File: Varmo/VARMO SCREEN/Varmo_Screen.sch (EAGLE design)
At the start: 34 parts, among them T1 MMBT2222AL, U1 LT1813CS8, U5 90814-0210

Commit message: Add PCA9670 to the schematic
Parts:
- removed R46, R47: 4.7k, rcl:R-EU_R0603
- added R20, R21: 4.7k, rcl:R-EU_R0603
- added R7: 100R, rcl:R-EU_R0603
- added U2: LT1813CS8, lineartechnology:LT1813CS8
- R1: value 100R -> 4.7k
- U1: value LT1813CS8 -> PCA9670D; device lineartechnology:LT1813CS8 -> NXP:PCA9670D
- renumbered C10 to C7, C4 to C1, C5 to C2, C6 to C3, C9 to C8, LCD1 to LCD2, LED6 to LED1, LED7 to LED2, LED8 to LED3, LED9 to LED4, R2 to R8, R25 to R13, R26 to R14, R29 to R15, R3 to R9, R30 to R16, R31 to R17, R4 to R10, R44 to R18, R45 to R19, R48 to R22, R49 to R23, R5 to R11, R50 to R24, R51 to R27, R6 to R12, T1 to T2, U$5 to U$1, U$7 to U$2, U5 to U3
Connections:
- removed net N$14: R10.2, R9.1, U1B.IN-
- removed net N$17: R10.1, R11.2, U1B.OUT
- removed net N$2: C1.1, R1.2, T2.B
- removed net N$3: R8.1, T2.C, U1A.IN+
- removed net N$5: R9.2, U1A.IN-, U1A.OUT
- new net N$1: C1.1, R7.2, T2.B
- new net N$6: R8.1, T2.C, U2A.IN+
- new net N$7: R9.2, U2A.IN-, U2A.OUT
- new net N$8: R10.2, R9.1, U2B.IN-
- new net N$9: R10.1, R11.2, U2B.OUT
- new net RESET: R1.1, U1.!RESET
- net +3V3: now also R1.2, R20.2, R21.2, U1.VDD; no longer R46.2, R47.2
- net +5V/1: now also U2A.V+; no longer U1A.V+
- net D0: now also U1.P0
- net D1: now also U1.P1
- net D2: now also U1.P2
- net D3: now also U1.P3
- net D4: now also U1.P4
- net D5: now also U1.P5
- net D6: now also U1.P6
- net D7: now also U1.P7
- net GND1: now also U1.AD0, U1.AD1, U1.VSS, U2B.IN+; no longer U1B.IN+
- net PWM_CONTRASTE: now also R7.1; no longer R1.1
- net SCL: now also R21.1, U1.SCL; no longer R47.1
- net SDA: now also R20.1, U1.SDA; no longer R46.1
- net VEE: now also U2A.V-; no longer U1A.V-
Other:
- note added: "I2C Adresse : 20h"

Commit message: Re routing the board
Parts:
- removed R20, R21: 4.7k, rcl:R-EU_R0603
- added R46, R47: 4.7k, rcl:R-EU_R0603
- R1: value 4.7k -> 100R
- R7: value 100R -> 4.7k
- U1: value PCA9670D -> LT1813CS8; device NXP:PCA9670D -> lineartechnology:LT1813CS8
- U2: value LT1813CS8 -> PCA9670D; device lineartechnology:LT1813CS8 -> NXP:PCA9670D
- renumbered C1 to C4, C2 to C5, C3 to C6, C7 to C10, C8 to C9, LCD2 to LCD1, LED1 to LED6, LED2 to LED7, LED3 to LED8, LED4 to LED9, R10 to R4, R11 to R5, R12 to R6, R13 to R25, R14 to R26, R15 to R29, R16 to R30, R17 to R31, R18 to R44, R19 to R45, R22 to R48, R23 to R49, R24 to R50, R27 to R51, R8 to R2, R9 to R3, T2 to T1, U$1 to U$5, U$2 to U$7, U3 to U5
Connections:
- removed net N$6: R2.1, T1.C, U2A.IN+
- removed net N$7: R3.2, U2A.IN-, U2A.OUT
- removed net N$8: R3.1, R4.2, U2B.IN-
- removed net N$9: R4.1, R5.2, U2B.OUT
- removed net RESET: R1.1, U1.!RESET
- new net N$14: R3.1, R4.2, U1B.IN-
- new net N$17: R4.1, R5.2, U1B.OUT
- new net N$2: C4.1, R1.2, T1.B
- new net N$3: R2.1, T1.C, U1A.IN+
- new net N$5: R3.2, U1A.IN-, U1A.OUT
- net +3V3: now also R46.2, R47.2, R7.2, U2.VDD; no longer R1.2, R20.2, R21.2, U1.VDD
- net +5V/1: now also U1A.V+; no longer U2A.V+
- net D0: now also U2.P0; no longer U1.P0
- net D1: now also U2.P1; no longer U1.P1
- net D2: now also U2.P2; no longer U1.P2
- net D3: now also U2.P3; no longer U1.P3
- net D4: now also U2.P4; no longer U1.P4
- net D5: now also U2.P5; no longer U1.P5
- net D6: now also U2.P6; no longer U1.P6
- net D7: now also U2.P7; no longer U1.P7
- net GND1: now also U1B.IN+, U2.AD0, U2.AD1, U2.AD2, U2.VSS; no longer U1.AD0, U1.AD1, U1.VSS, U2B.IN+
- net N$1: now also R7.1, U2.!RESET; no longer C4.1, R7.2, T1.B
- net PWM_CONTRASTE: now also R1.1; no longer R7.1
- net SCL: now also R47.1, U2.SCL; no longer R21.1, U1.SCL
- net SDA: now also R46.1, U2.SDA; no longer R20.1, U1.SDA
- net VEE: now also U1A.V-; no longer U2A.V-
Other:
- moved on the sheet: R1, R7

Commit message: Update the LT1813 devide
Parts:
- U1: value LT1813CS8 -> LT1813; device lineartechnology:LT1813CS8 -> lineartechnology:LT1813
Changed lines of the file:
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@@
 <parts>
 <part name="FRAME2" library="frames" deviceset="A3L-LOC" device=""/>
-<part name="U1" library="lineartechnology" deviceset="LT1813" device="CS8"/>
+<part name="U1" library="lineartechnology" deviceset="LT1813" device=""/>
 <part name="T1" library="transistor" deviceset="MMBT2222AL" device=""/>
 <part name="R1" library="rcl" deviceset="R-EU_" device="R0603" value="100R"/>

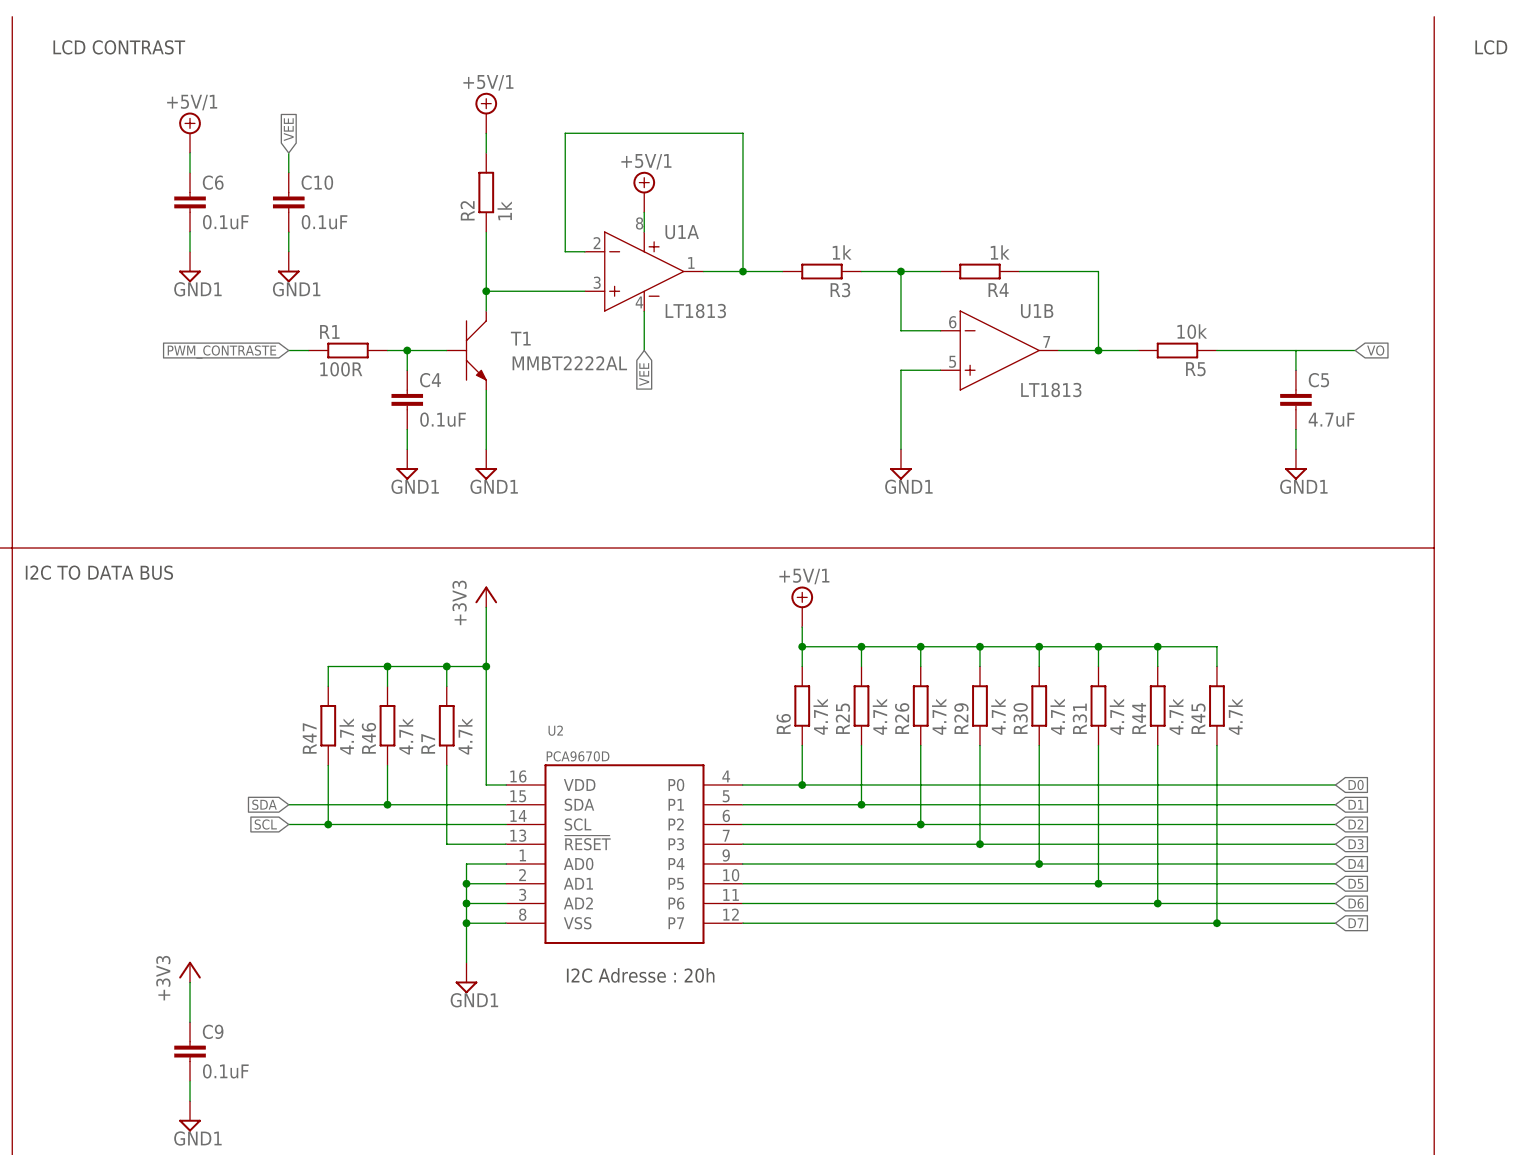
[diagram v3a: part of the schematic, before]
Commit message: Add TLP0401A to the schematic and route the board
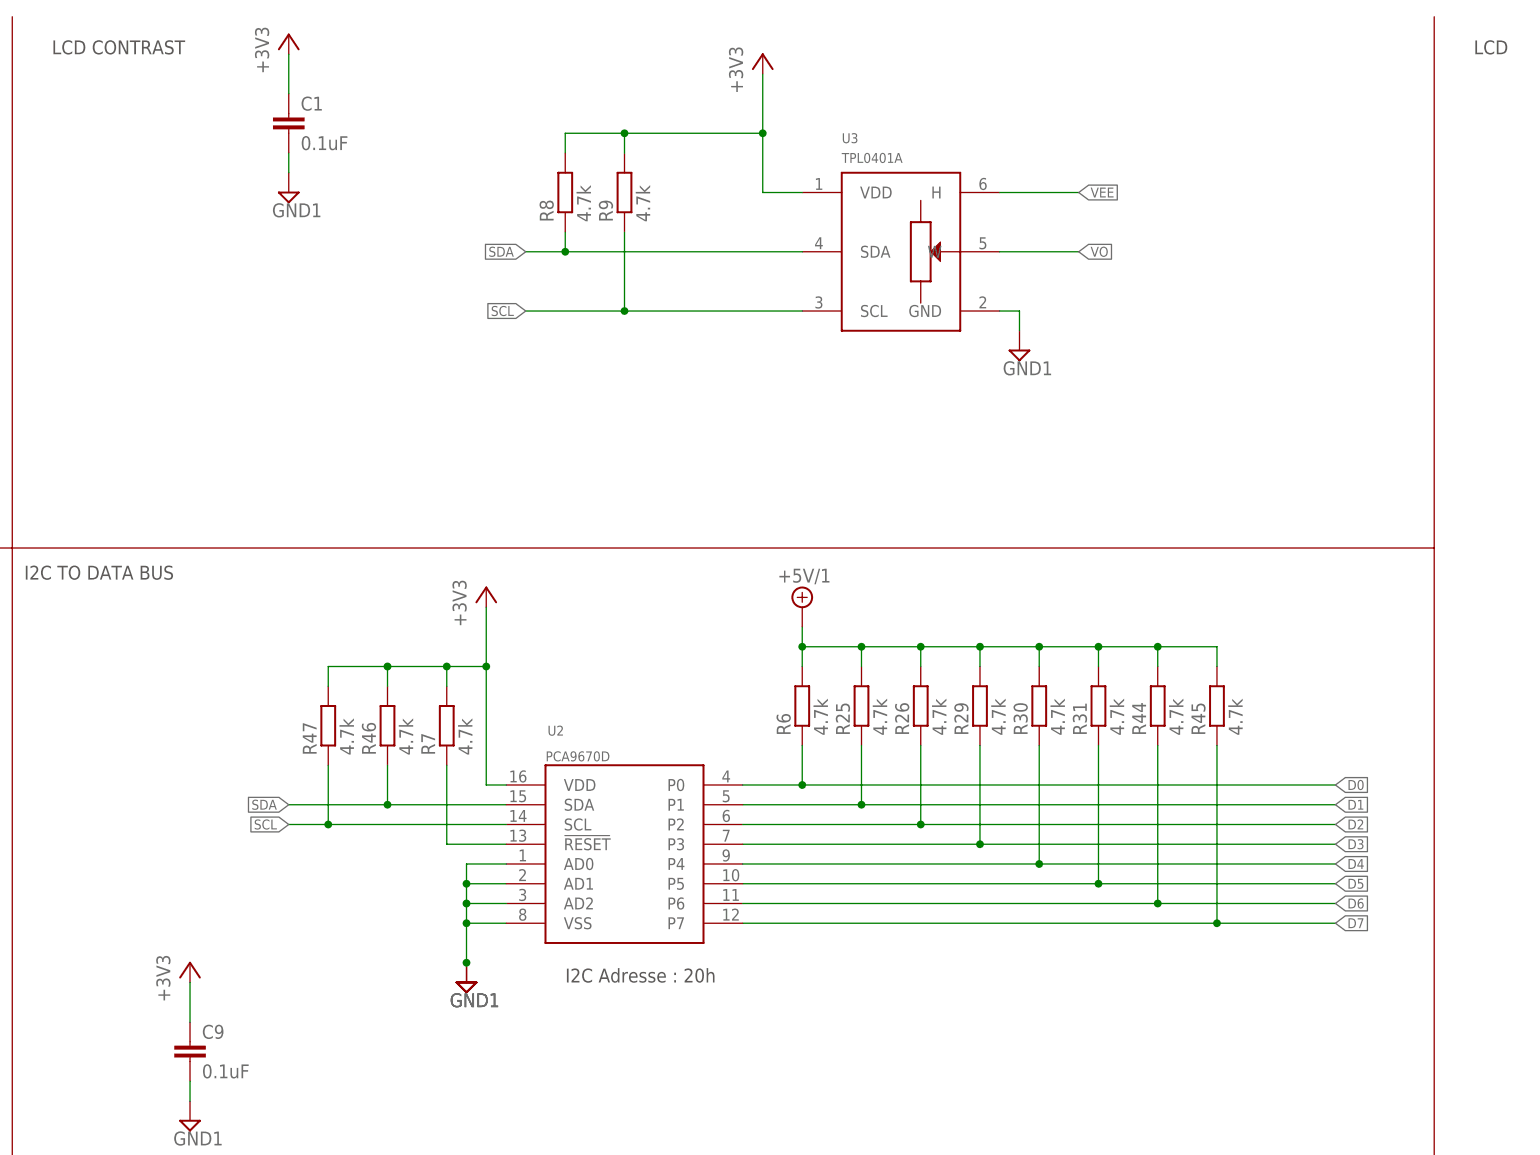
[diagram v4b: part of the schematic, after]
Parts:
- removed C10, C4, C6: 0.1uF, rcl:C-EUC0603
- removed C5: 4.7uF, rcl:C-EUC0603
- removed R1: 100R, rcl:R-EU_R0603
- removed R2, R3, R4: 1k, rcl:R-EU_R0603
- removed R5: 10k, rcl:R-EU_R0603
- removed T1: MMBT2222AL, transistor:MMBT2222AL
- removed U1: LT1813, lineartechnology:LT1813
- added C1: 0.1uF, rcl:C-EUC0603
- added R8, R9: 4.7k, rcl:R-EU_R0603
- added U3: TPL0401A, ti:TPL0401A
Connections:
- removed net N$14: R3.1, R4.2, U1B.IN-
- removed net N$17: R4.1, R5.2, U1B.OUT
- removed net N$2: C4.1, R1.2, T1.B
- removed net N$3: R2.1, T1.C, U1A.IN+
- removed net N$5: R3.2, U1A.IN-, U1A.OUT
- net +3V3: now also C1.1, R8.2, R9.2, U3.VDD
- net +5V/1: no longer C6.1, R2.2, U1A.V+
- net GND1: now also C1.2, U3.GND; no longer C10.2, C4.2, C5.2, C6.2, T1.E, U1B.IN+
- net PWM_CONTRASTE: no longer R1.1
- net SCL: now also R9.1, U3.SCL
- net SDA: now also R8.1, U3.SDA
- net VEE: now also U3.H; no longer C10.1, U1A.V-
- net VO: now also U3.W; no longer C5.1, R5.1

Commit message: Add manuel potentiometer
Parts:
- added R1: 3313J-1-103E, pot:3313J-1-103E
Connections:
- net GND1: now also R1.A
- net VEE: now also R1.E
- net VO: now also R1.S
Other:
- note added: "I2C Adresse : 2Eh"
- note added: "NC"
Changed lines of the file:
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@@
 <part name="R8" library="rcl" deviceset="R-EU_" device="R0603" value="4.7k"/>
 <part name="R9" library="rcl" deviceset="R-EU_" device="R0603" value="4.7k"/>
+<part name="R1" library="pot" deviceset="3313J" device="" technology="-1-103E"/>
+<part name="SUPPLY4" library="supply2" deviceset="GND1" device=""/>
 </parts>
 <sheets>
@@
 <text x="292.1" y="251.46" size="1.778" layer="97">LCD</text>
 <text x="175.26" y="132.08" size="1.778" layer="97">I2C Adresse : 20h</text>
+<text x="210.82" y="203.2" size="1.778" layer="97">I2C Adresse : 2Eh</text>
+<text x="266.7" y="223.52" size="1.778" layer="97">NC</text>
 </plain>
 <instances>
@@
 <instance part="R8" gate="G$1" x="175.26" y="233.68" rot="R90"/>
 <instance part="R9" gate="G$1" x="182.88" y="233.68" rot="R90"/>
+<instance part="R1" gate="G$1" x="264.16" y="228.6"/>
+<instance part="SUPPLY4" gate="G$1" x="264.16" y="213.36"/>
 </instances>
 <busses>
@@
 <label x="241.3" y="226.06" size="1.27" layer="95" xref="yes"/>
 <pinref part="U3" gate="G$1" pin="W"/>
+</segment>
+<segment>
+<wire x1="274.32" y1="228.6" x2="269.24" y2="228.6" width="0.1524" layer="91"/>
+<pinref part="R1" gate="G$1" pin="S"/>
+<label x="274.32" y="228.6" size="1.27" layer="95" xref="yes"/>
 </segment>
 </net>
@@
 <wire x1="139.7" y1="236.22" x2="139.7" y2="238.76" width="0.1524" layer="91"/>
 </segment>
+<segment>
+<pinref part="SUPPLY4" gate="G$1" pin="GND1"/>
+<pinref part="R1" gate="G$1" pin="A"/>
+<wire x1="264.16" y1="215.9" x2="264.16" y2="223.52" width="0.1524" layer="91"/>
+</segment>
 </net>
 <net name="VEE" class="0">
@@
 <label x="241.3" y="233.68" size="1.27" layer="95" xref="yes"/>
 </segment>
-</net>
+<segment>
+<wire x1="274.32" y1="241.3" x2="264.16" y2="241.3" width="0.1524" layer="91"/>
+<pinref part="R1" gate="G$1" pin="E"/>
+<wire x1="264.16" y1="233.68" x2="264.16" y2="241.3" width="0.1524" layer="91"/>
+<label x="274.32" y="241.3" size="1.27" layer="95" xref="yes"/>
+</segment>
+</net>
